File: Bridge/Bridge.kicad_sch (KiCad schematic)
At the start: 31 parts, among them J1 Conn_01x01_Pin, J2 Conn_01x01_Pin, J3 Conn_01x01_Pin, J4 Conn_01x02_Pin, J5 Barrel_Jack, Q1 BUZ11, Q2 BUZ11, U1 74132, U2 TLP250, U3 TLP250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

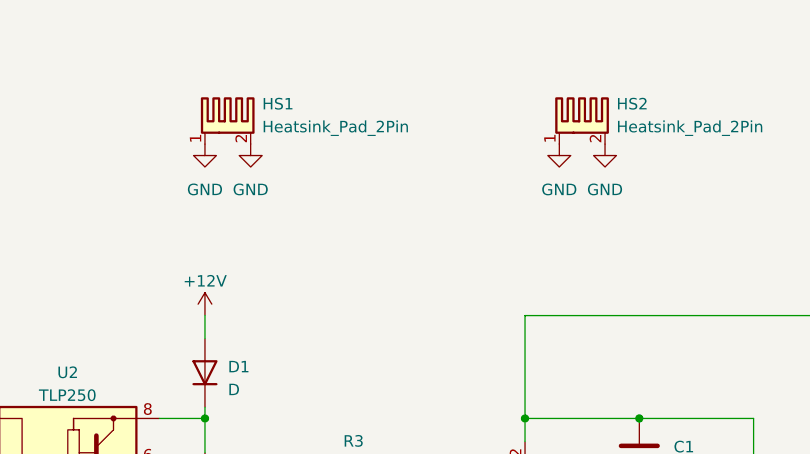
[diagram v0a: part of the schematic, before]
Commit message: edit silkscreen
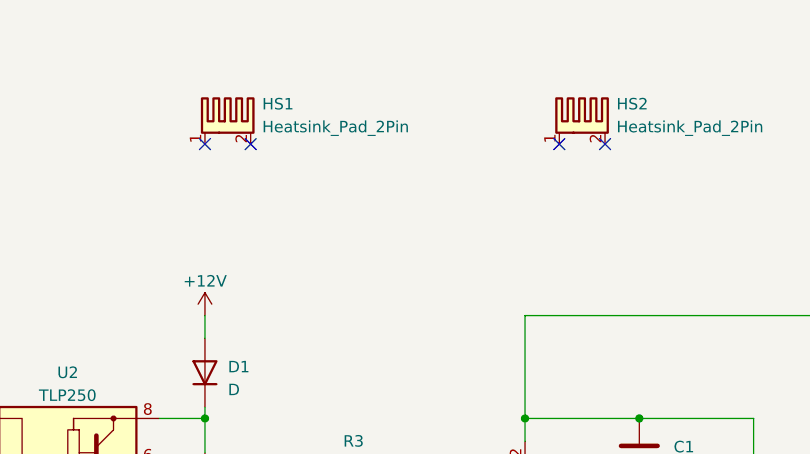
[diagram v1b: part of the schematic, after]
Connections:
- net GND: no longer HS1.1, HS1.2, HS2.1, HS2.2
- no-connect marks 0 -> 4
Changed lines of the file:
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@@
   (junction (at 215.9 114.3) (diameter 0) (color 0 0 0 0)
   )
+  (no_connect (at 219.71 57.15))
+  (no_connect (at 224.79 57.15))
+  (no_connect (at 180.34 57.15))
+  (no_connect (at 185.42 57.15))
   (wire (pts (xy 39.37 55.88) (xy 36.83 55.88))
     (stroke (width 0) (type default))
@@
         (path "/7b1c29b2-aaa9-4950-8c77-d7ab4040900b"
           (reference "#PWR013") (unit 1)
-        )
-      )
-    )
-  )
-  (symbol (lib_id "power:GND") (at 185.42 57.15 0) (unit 1)
-    (in_bom yes) (on_board yes) (dnp no) (fields_autoplaced)
-    (property "Reference" "#PWR02" (at 185.42 63.5 0)
-      (effects (font (size 1.27 1.27)) hide)
-    )
-    (property "Value" "GND" (at 185.42 62.23 0)
-      (effects (font (size 1.27 1.27)))
-    )
-    (property "Footprint" "" (at 185.42 57.15 0)
-      (effects (font (size 1.27 1.27)) hide)
-    )
-    (property "Datasheet" "" (at 185.42 57.15 0)
-      (effects (font (size 1.27 1.27)) hide)
-    )
-    (pin "1")
-    (instances
-      (project "Bridge"
-        (path "/7b1c29b2-aaa9-4950-8c77-d7ab4040900b"
-          (reference "#PWR02") (unit 1)
         )
       )
@@
     )
   )
-  (symbol (lib_id "power:GND") (at 219.71 57.15 0) (unit 1)
-    (in_bom yes) (on_board yes) (dnp no) (fields_autoplaced)
-    (property "Reference" "#PWR03" (at 219.71 63.5 0)
-      (effects (font (size 1.27 1.27)) hide)
-    )
-    (property "Value" "GND" (at 219.71 62.23 0)
-      (effects (font (size 1.27 1.27)))
-    )
-    (property "Footprint" "" (at 219.71 57.15 0)
-      (effects (font (size 1.27 1.27)) hide)
-    )
-    (property "Datasheet" "" (at 219.71 57.15 0)
-      (effects (font (size 1.27 1.27)) hide)
-    )
-    (pin "1")
-    (instances
-      (project "Bridge"
-        (path "/7b1c29b2-aaa9-4950-8c77-d7ab4040900b"
-          (reference "#PWR03") (unit 1)
-        )
-      )
-    )
-  )
   (symbol (lib_id "Device:C") (at 101.6 107.95 0) (unit 1)
     (in_bom yes) (on_board yes) (dnp no) (fields_autoplaced)
@@
         (path "/7b1c29b2-aaa9-4950-8c77-d7ab4040900b"
           (reference "HS2") (unit 1)
-        )
-      )
-    )
-  )
-  (symbol (lib_id "power:GND") (at 180.34 57.15 0) (unit 1)
-    (in_bom yes) (on_board yes) (dnp no) (fields_autoplaced)
-    (property "Reference" "#PWR01" (at 180.34 63.5 0)
-      (effects (font (size 1.27 1.27)) hide)
-    )
-    (property "Value" "GND" (at 180.34 62.23 0)
-      (effects (font (size 1.27 1.27)))
-    )
-    (property "Footprint" "" (at 180.34 57.15 0)
-      (effects (font (size 1.27 1.27)) hide)
-    )
-    (property "Datasheet" "" (at 180.34 57.15 0)
-      (effects (font (size 1.27 1.27)) hide)
-    )
-    (pin "1")
-    (instances
-      (project "Bridge"
-        (path "/7b1c29b2-aaa9-4950-8c77-d7ab4040900b"
-          (reference "#PWR01") (unit 1)
         )
       )
@@
         )
       )
-    )
-  )
-  (symbol (lib_id "power:GND") (at 224.79 57.15 0) (unit 1)
-    (in_bom yes) (on_board yes) (dnp no) (fields_autoplaced)
-    (property "Reference" "#PWR04" (at 224.79 63.5 0)
-      (effects (font (size 1.27 1.27)) hide)
-    )
-    (property "Value" "GND" (at 224.79 62.23 0)
-      (effects (font (size 1.27 1.27)))
-    )
-    (property "Footprint" "" (at 224.79 57.15 0)
-      (effects (font (size 1.27 1.27)) hide)
-    )
-    (property "Datasheet" "" (at 224.79 57.15 0)
-      (effects (font (size 1.27 1.27)) hide)
-    )
-    (pin "1")
-    (instances
-      (project "Bridge"
-        (path "/7b1c29b2-aaa9-4950-8c77-d7ab4040900b"
-          (reference "#PWR04") (unit 1)
-        )
-      )
